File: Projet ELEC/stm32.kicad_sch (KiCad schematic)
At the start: 13 parts, among them SW1 SW_Push, U8 STM32F103RBTx

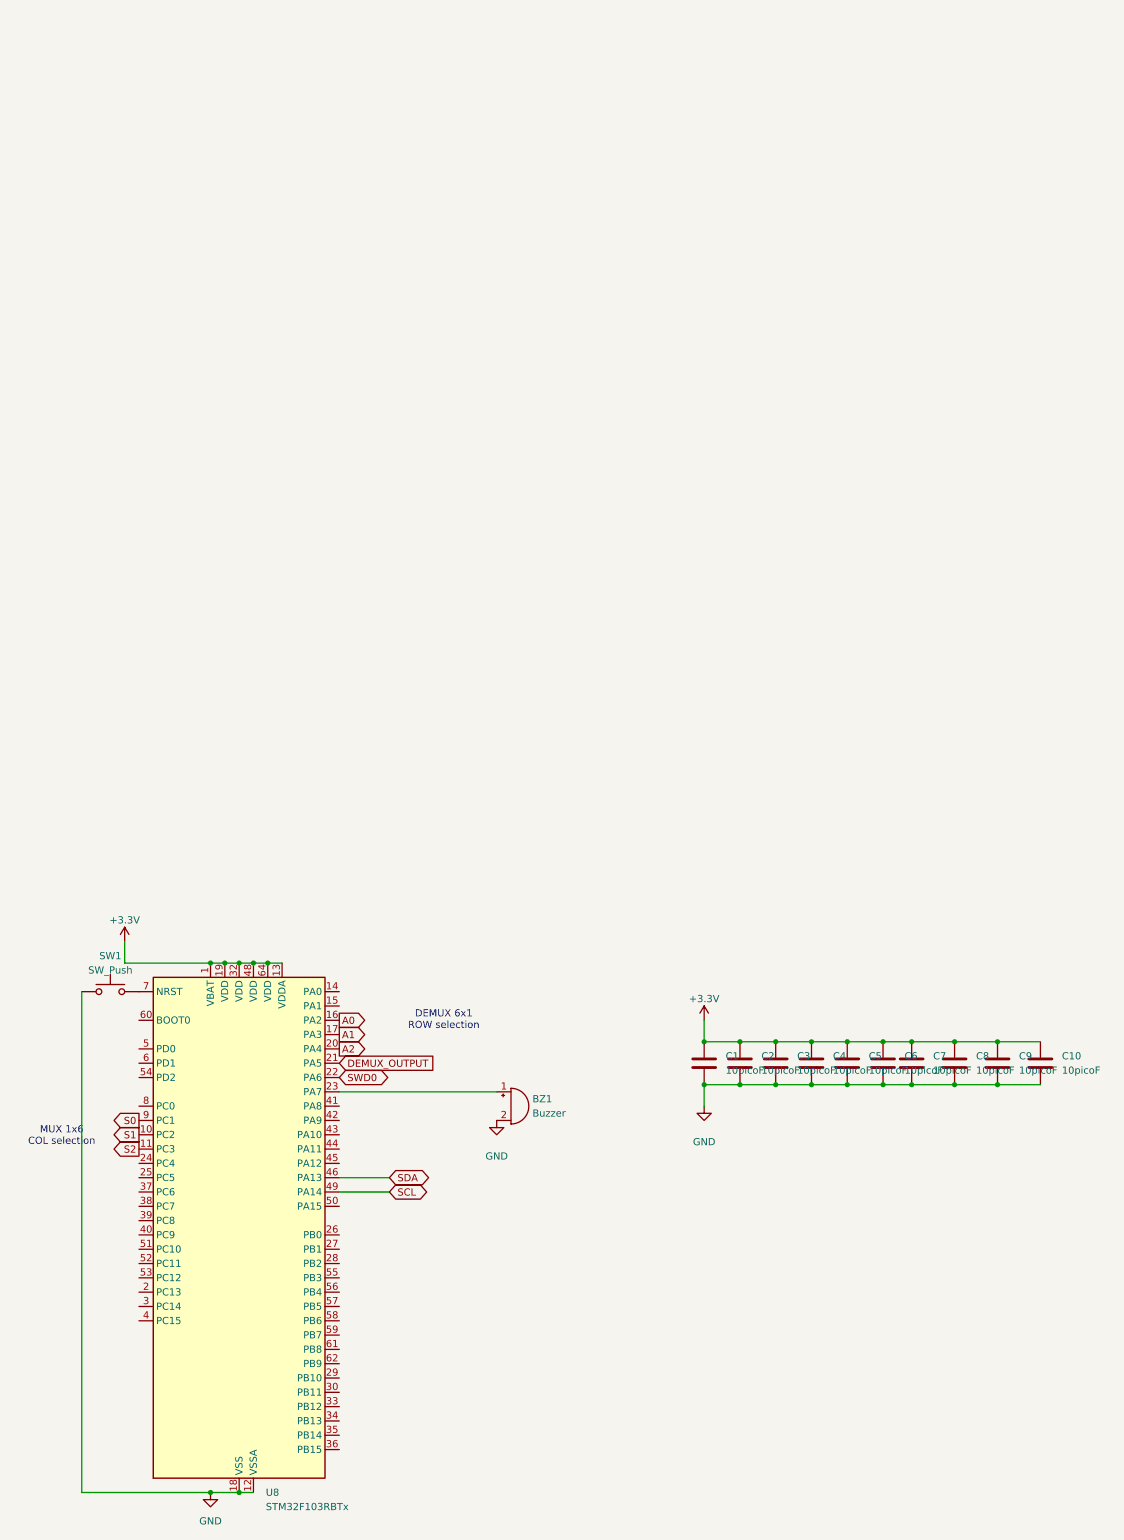
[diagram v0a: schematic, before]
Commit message: feat(stm32): schematics for f103
* Projet ELEC/stm32.kicad_sch
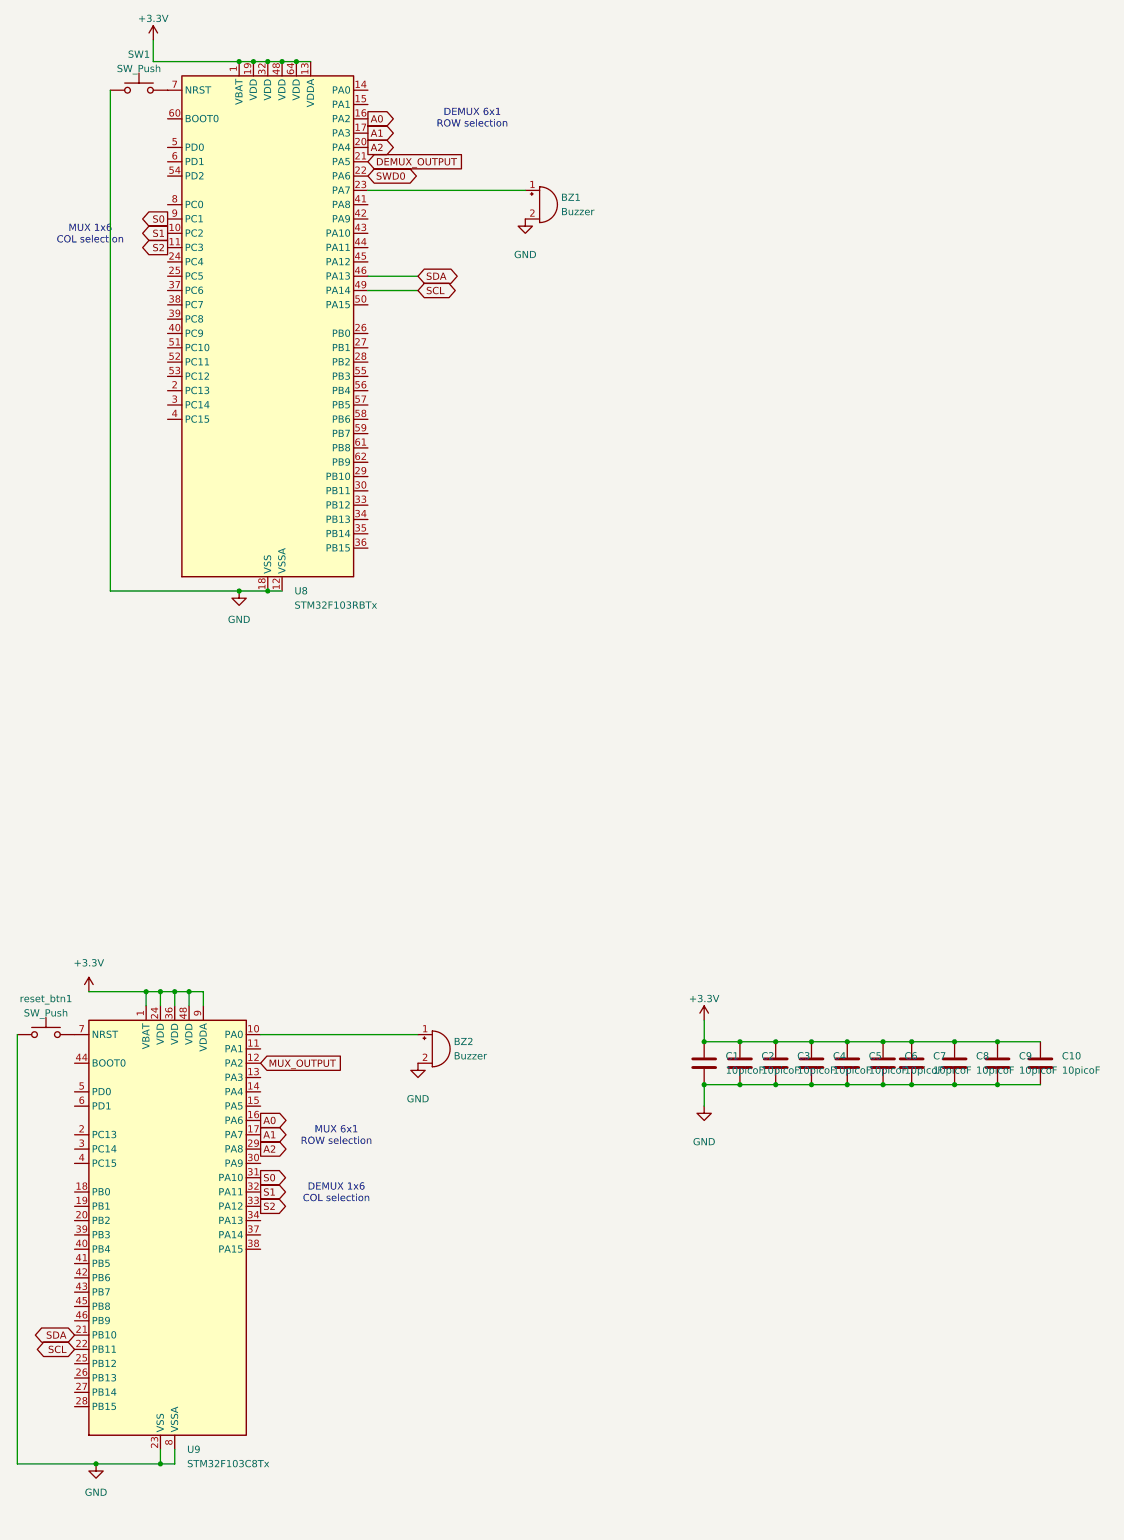
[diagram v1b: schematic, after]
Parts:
- added BZ2: Buzzer, Buzzer_Beeper:Buzzer_TDK_PS1240P02BT_D12.2mm_H6.5mm, symbol Device:Buzzer
- added U9: STM32F103C8Tx, Package_QFP:LQFP-48_7x7mm_P0.5mm, symbol MCU_ST_STM32F1:STM32F103C8Tx
- added reset_btn1: SW_Push, Button_Switch_SMD:SW_Push_1P1T_NO_CK_PTS125Sx43PSMTR, symbol Switch:SW_Push
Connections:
- net +3.3V: now also U9.1 (VBAT), U9.24 (VDD), U9.36 (VDD), U9.48 (VDD), U9.9 (VDDA)
- net A0: now also U9.16 (PA6)
- net A1: now also U9.17 (PA7)
- net A2: now also U9.29 (PA8)
- net GND: now also BZ2.2 (-), U9.23 (VSS), U9.35 (VSS), U9.47 (VSS), U9.8 (VSSA), reset_btn1.1
- net S0: now also U9.31 (PA10)
- net S1: now also U9.32 (PA11)
- net S2: now also U9.33 (PA12)
- net SCL: now also U9.22 (PB11)
- net SDA: now also U9.21 (PB10)
- new net: U9.7 (NRST), reset_btn1.2
- new net: BZ2.1 (+), U9.10 (PA0)
- new net MUX_OUTPUT: U9.12 (PA2)
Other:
- note added: "DEMUX 1x6 COL selection"
- note added: "MUX 6x1 ROW selection"
- moved on the sheet: BZ1, SW1, U8
